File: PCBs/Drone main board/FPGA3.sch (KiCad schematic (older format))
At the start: 11 parts, among them U1201 10CL040_F484, X1401 SiT2001B1-S2-33E-50

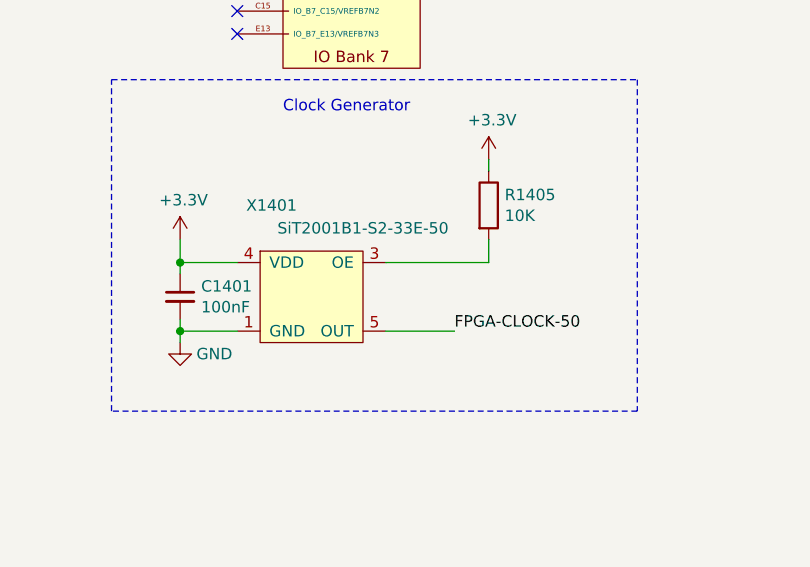
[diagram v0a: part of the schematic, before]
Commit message: Minor tweaks. Improved groundplane around FPGA core (removed and relocated a few power vias) and flipped clock circuit to the same side as the FPGA.
Signed-off-by: Eldalote.Electronics <Eldalote.Electronics@gmail.com>
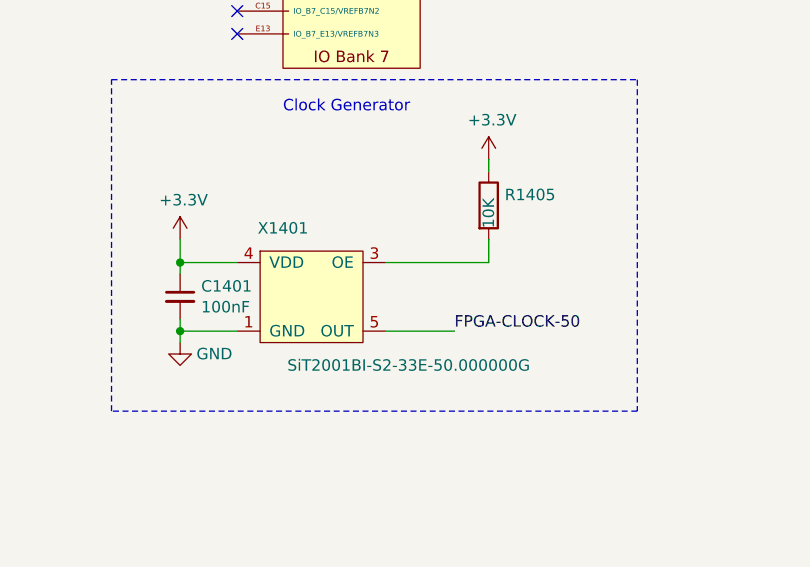
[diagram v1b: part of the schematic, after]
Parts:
- C1401: footprint Inductor_SMD:L_0402_1005Metric -> Inductor_SMD:L_0603_1608Metric_Pad1.05x0.95mm_HandSolder; DigiKey (none) -> 732-13187-1-ND; LCSC C1525 -> (none); Mouser (none) -> 710-885382206004
- X1401: value SiT2001B1-S2-33E-50 -> SiT2001BI-S2-33E-50.000000G; DigiKey (none) -> 1473-SIT2001BI-S2-33E-50.000000G-ND; Mouser (none) -> 788-2001BI-S233E-50G
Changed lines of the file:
@@
 U 1 1 5FC5708A
 P 8200 5400
-F 0 "X1401" H 8200 5300 50  0000 C CNN
-F 1 "SiT2001B1-S2-33E-50" H 8600 5200 50  0000 C CNN
+F 0 "X1401" H 8250 5200 50  0000 C CNN
+F 1 "SiT2001BI-S2-33E-50.000000G" H 8800 4600 50  0000 C CNN
 F 2 "Package_TO_SOT_SMD:SOT-23-5_HandSoldering" H 8200 5400 50  0001 C CNN
 F 3 "" H 8200 5400 50  0001 C CNN
+F 4 "1473-SIT2001BI-S2-33E-50.000000G-ND " H 8200 5400 50  0001 C CNN "DigiKey"
+F 5 "788-2001BI-S233E-50G " H 8200 5400 50  0001 C CNN "Mouser"
 	1    8200 5400
 	1    0    0    -1
@@
 F 0 "C1401" H 7892 5946 50  0000 L CNN
 F 1 "100nF" H 7892 5855 50  0000 L CNN
-F 2 "Inductor_SMD:L_0402_1005Metric" H 7800 5900 50  0001 C CNN
+F 2 "Inductor_SMD:L_0603_1608Metric_Pad1.05x0.95mm_HandSolder" H 7800 5900 50  0001 C CNN
 F 3 "~" H 7800 5900 50  0001 C CNN
-F 4 "" H 7800 5900 50  0001 C CNN "DigiKey"
-F 5 "" H 7800 5900 50  0001 C CNN "Mouser"
-F 6 "C1525" H 7800 5900 50  0001 C CNN "LCSC"
+F 4 "732-13187-1-ND " H 7800 5900 50  0001 C CNN "DigiKey"
+F 5 "710-885382206004" H 7800 5900 50  0001 C CNN "Mouser"
 	1    7800 5900
 	1    0    0    -1
@@
 AR Path="/5F48BB5C/5FC89410" Ref="R1405"  Part="1"
 F 0 "R1405" H 9220 5546 50  0000 L CNN
-F 1 "10K" H 9220 5455 50  0000 L CNN
+F 1 "10K" V 9150 5400 50  0000 L CNN
 F 2 "Resistor_SMD:R_0402_1005Metric" V 9080 5500 50  0001 C CNN
 F 3 "~" H 9150 5500 50  0001 C CNN

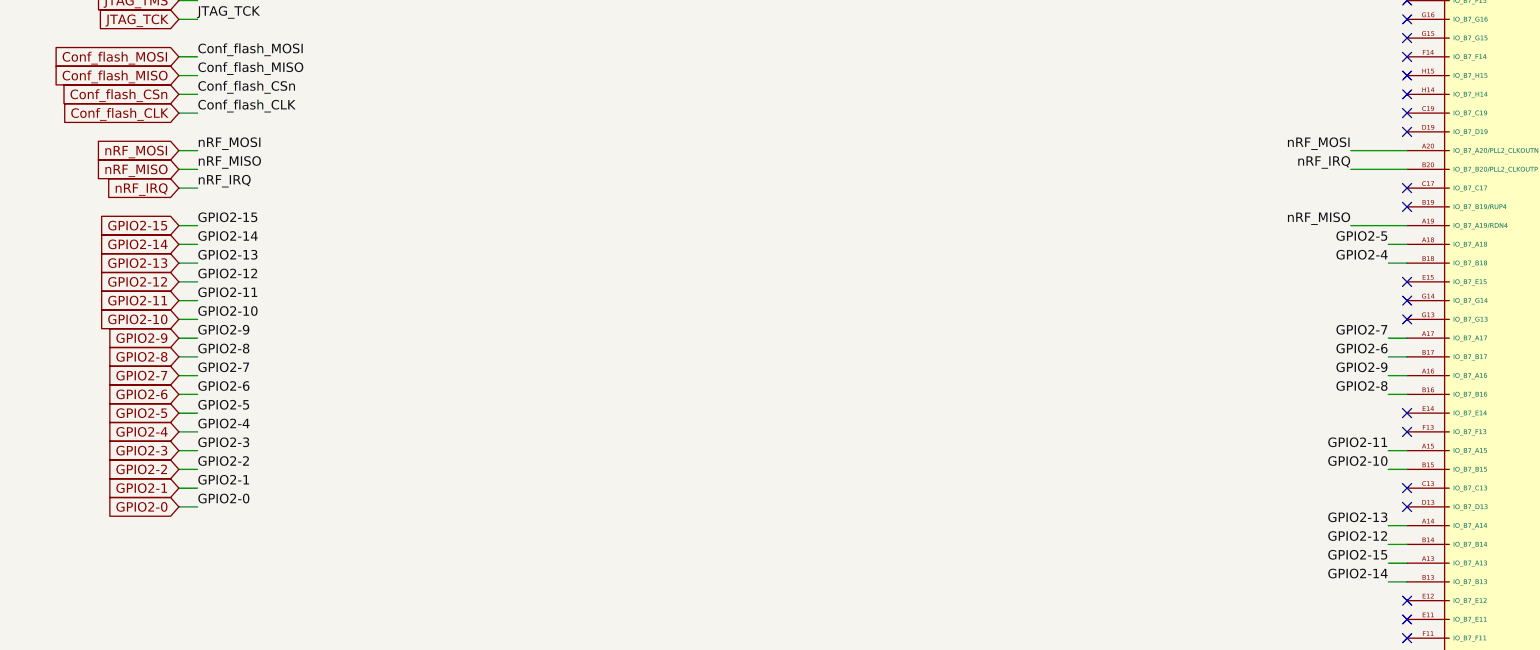
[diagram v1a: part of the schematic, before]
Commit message: Finished (?) the schematic check and update. Next: PCB update
Signed-off-by: Eldalote.Electronics <Eldalote.Electronics@gmail.com>
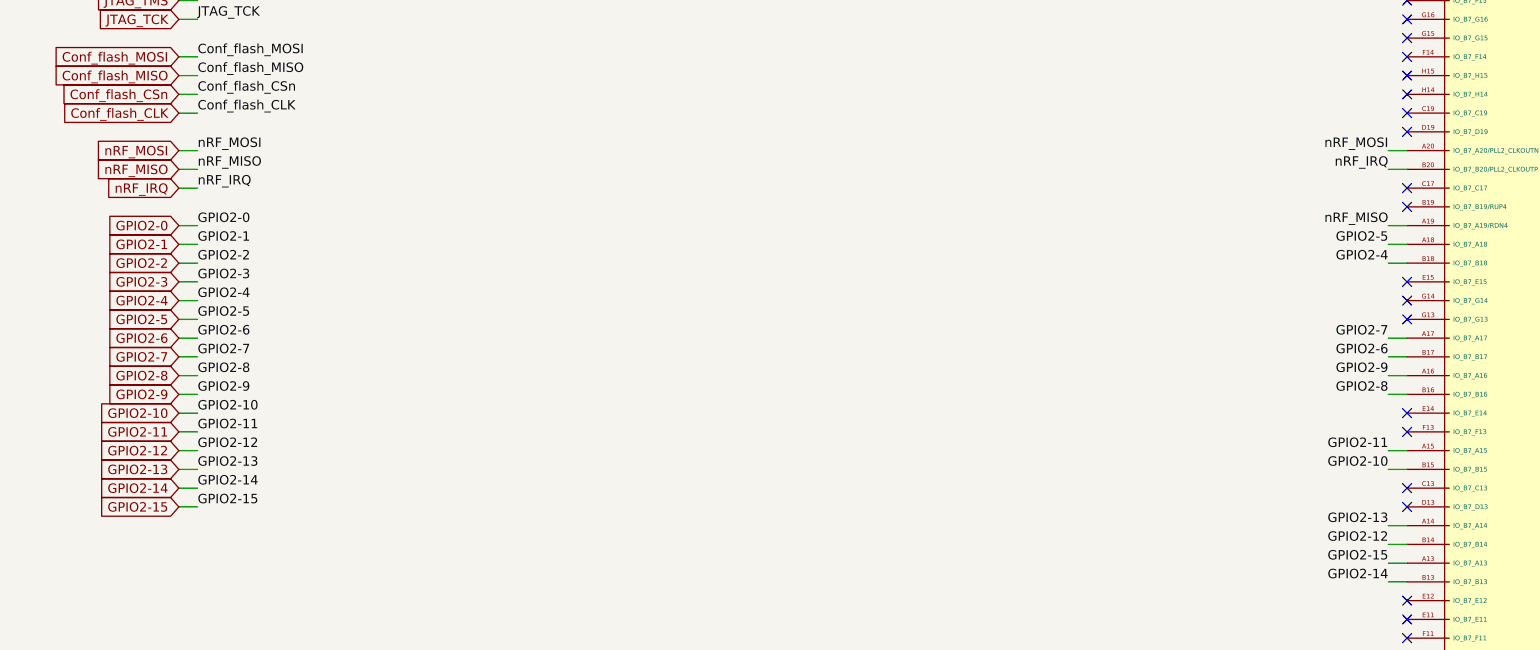
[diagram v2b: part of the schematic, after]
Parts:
- C1401: footprint Inductor_SMD:L_0603_1608Metric_Pad1.05x0.95mm_HandSolder -> Inductor_SMD:L_0402_1005Metric; DigiKey 732-13187-1-ND -> (none); MfNr (none) -> CL05B104KO5NNNC; Mouser 710-885382206004 -> (none)
- R1401, R1402, R1403, R1404, R1405: LCSC C25744 -> (none); MfNr (none) -> RC0402FR-0710KL
- U1201: MfNr (none) -> 10CL040Y
- X1401: footprint Package_TO_SOT_SMD:SOT-23-5_HandSoldering -> Package_TO_SOT_SMD:SOT-23-5; DigiKey 1473-SIT2001BI-S2-33E-50.000000G-ND -> (none); MfNr (none) -> SIT2001BI-S2-33E-50.000000G; Mouser 788-2001BI-S233E-50G -> (none)
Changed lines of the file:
@@
 F 4 "TRUE" H 9300 -5415 35  0001 L CNN "SPLIT_INST"
 F 5 "(S1+S2+S3+S4+S5+S6+S7+S8+S9+S10+S11+S12+S13)" H 9300 -5460 35  0001 L CNN "SWAP_INFO"
+F 6 "10CL040Y" H 8250 600 50  0001 C CNN "MfNr"
 	8    8250 600
 	1    0    0    -1
@@
 F 4 "TRUE" H 11500 -5415 35  0001 L CNN "SPLIT_INST"
 F 5 "(S1+S2+S3+S4+S5+S6+S7+S8+S9+S10+S11+S12+S13)" H 11500 -5460 35  0001 L CNN "SWAP_INFO"
+F 6 "10CL040Y" H 10450 600 50  0001 C CNN "MfNr"
 	9    10450 600
 	1    0    0    -1
@@
 F 4 "TRUE" H 7150 -665 35  0001 L CNN "SPLIT_INST"
 F 5 "(S1+S2+S3+S4+S5+S6+S7+S8+S9+S10+S11+S12+S13)" H 7150 -710 35  0001 L CNN "SWAP_INFO"
+F 6 "10CL040Y" H 6100 5350 50  0001 C CNN "MfNr"
 	10   6100 5350
 	1    0    0    -1
@@
 F 4 "TRUE" H 3100 -815 35  0001 L CNN "SPLIT_INST"
 F 5 "(S1+S2+S3+S4+S5+S6+S7+S8+S9+S10+S11+S12+S13)" H 3100 -860 35  0001 L CNN "SWAP_INFO"
+F 6 "10CL040Y" H 2050 5200 50  0001 C CNN "MfNr"
 	11   2050 5200
 	1    0    0    -1
@@
 F 2 "Resistor_SMD:R_0402_1005Metric" V 4080 5500 50  0001 C CNN
 F 3 "~" H 4150 5500 50  0001 C CNN
-F 4 "C25744" V 4150 5500 50  0001 C CNN "LCSC"
+F 4 "RC0402FR-0710KL" V 4150 5500 50  0001 C CNN "MfNr"
 	1    4150 5500
 	-1   0    0    1
@@
 F 2 "Resistor_SMD:R_0402_1005Metric" V 4280 5600 50  0001 C CNN
 F 3 "~" H 4350 5600 50  0001 C CNN
-F 4 "C25744" V 4350 5600 50  0001 C CNN "LCSC"
+F 4 "RC0402FR-0710KL" V 4350 5600 50  0001 C CNN "MfNr"
 	1    4350 5600
 	-1   0    0    1
@@
 F 2 "Resistor_SMD:R_0402_1005Metric" V 1380 5300 50  0001 C CNN
 F 3 "~" H 1450 5300 50  0001 C CNN
-F 4 "C25744" V 1450 5300 50  0001 C CNN "LCSC"
+F 4 "RC0402FR-0710KL" V 1450 5300 50  0001 C CNN "MfNr"
 	1    1450 5300
 	-1   0    0    1
@@
 nRF_IRQ
 Wire Wire Line
-	8050 2050 7750 2050
-Wire Wire Line
-	8050 1650 7750 1650
-Wire Wire Line
-	8050 1750 7750 1750
-Text Label 7750 1650 2    50   ~ 0
+	8050 2050 7950 2050
+Wire Wire Line
+	8050 1650 7950 1650
+Wire Wire Line
+	8050 1750 7950 1750
+Text Label 7950 1650 2    50   ~ 0
 nRF_MOSI
-Text Label 7750 1750 2    50   ~ 0
+Text Label 7950 1750 2    50   ~ 0
 nRF_IRQ
-Text Label 7750 2050 2    50   ~ 0
+Text Label 7950 2050 2    50   ~ 0
 nRF_MISO
 $Comp
@@
 F 2 "Resistor_SMD:R_0402_1005Metric" V 4580 6050 50  0001 C CNN
 F 3 "~" H 4650 6050 50  0001 C CNN
-F 4 "C25744" V 4650 6050 50  0001 C CNN "LCSC"
+F 4 "RC0402FR-0710KL" V 4650 6050 50  0001 C CNN "MfNr"
 	1    4650 6050
 	-1   0    0    1
@@
 ~CE
 Wire Wire Line
-	1500 3550 1600 3550
+	1500 2050 1600 2050
+Wire Wire Line
+	1600 2150 1500 2150
+Wire Wire Line
+	1600 2250 1500 2250
+Wire Wire Line
+	1600 2350 1500 2350
+Wire Wire Line
+	1600 2450 1500 2450
+Wire Wire Line
+	1600 2550 1500 2550
+Wire Wire Line
+	1600 2650 1500 2650
+Wire Wire Line
+	1600 2750 1500 2750
+Wire Wire Line
+	1600 2850 1500 2850
+Wire Wire Line
+	1600 2950 1500 2950
+Wire Wire Line
+	1600 3050 1500 3050
+Wire Wire Line
+	1600 3150 1500 3150
+Wire Wire Line
+	1600 3250 1500 3250
+Wire Wire Line
+	1600 3350 1500 3350
 Wire Wire Line
 	1600 3450 1500 3450
 Wire Wire Line
-	1600 3350 1500 3350
-Wire Wire Line
-	1600 3250 1500 3250
-Wire Wire Line
-	1600 3150 1500 3150
-Wire Wire Line
-	1600 3050 1500 3050
-Wire Wire Line
-	1600 2950 1500 2950
-Wire Wire Line
-	1600 2850 1500 2850
-Wire Wire Line
-	1600 2750 1500 2750
-Wire Wire Line
-	1600 2650 1500 2650
-Wire Wire Line
-	1600 2550 1500 2550
-Wire Wire Line
-	1600 2450 1500 2450
-Wire Wire Line
-	1600 2350 1500 2350
-Wire Wire Line
-	1600 2250 1500 2250
-Wire Wire Line
-	1600 2150 1500 2150
-Wire Wire Line
-	1600 2050 1500 2050
+	1600 3550 1500 3550
+Text Label 1600 2050 0    50   ~ 0
+GPIO2-0
+Text Label 1600 2150 0    50   ~ 0
+GPIO2-1
+Text Label 1600 2250 0    50   ~ 0
+GPIO2-2
+Text Label 1600 2350 0    50   ~ 0
+GPIO2-3
+Text Label 1600 2450 0    50   ~ 0
+GPIO2-4
+Text Label 1600 2550 0    50   ~ 0
+GPIO2-5
+Text Label 1600 2650 0    50   ~ 0
+GPIO2-6
+Text Label 1600 2750 0    50   ~ 0
+GPIO2-7
+Text Label 1600 2850 0    50   ~ 0
+GPIO2-8
+Text Label 1600 2950 0    50   ~ 0
+GPIO2-9
+Text Label 1600 3050 0    50   ~ 0
+GPIO2-10
+Text Label 1600 3150 0    50   ~ 0
+GPIO2-11
+Text Label 1600 3250 0    50   ~ 0
+GPIO2-12
+Text Label 1600 3350 0    50   ~ 0
+GPIO2-13
+Text Label 1600 3450 0    50   ~ 0
+GPIO2-14
 Text Label 1600 3550 0    50   ~ 0
+GPIO2-15
+Text GLabel 1500 2050 0    50   Input ~ 0
 GPIO2-0
-Text Label 1600 3450 0    50   ~ 0
+Text GLabel 1500 2150 0    50   Input ~ 0
 GPIO2-1
-Text Label 1600 3350 0    50   ~ 0
+Text GLabel 1500 2250 0    50   Input ~ 0
 GPIO2-2
-Text Label 1600 3250 0    50   ~ 0
+Text GLabel 1500 2350 0    50   Input ~ 0
 GPIO2-3
-Text Label 1600 3150 0    50   ~ 0
+Text GLabel 1500 2450 0    50   Input ~ 0
 GPIO2-4
-Text Label 1600 3050 0    50   ~ 0
+Text GLabel 1500 2550 0    50   Input ~ 0
 GPIO2-5
-Text Label 1600 2950 0    50   ~ 0
+Text GLabel 1500 2650 0    50   Input ~ 0
 GPIO2-6
-Text Label 1600 2850 0    50   ~ 0
+Text GLabel 1500 2750 0    50   Input ~ 0
 GPIO2-7
-Text Label 1600 2750 0    50   ~ 0
+Text GLabel 1500 2850 0    50   Input ~ 0
 GPIO2-8
-Text Label 1600 2650 0    50   ~ 0
+Text GLabel 1500 2950 0    50   Input ~ 0
 GPIO2-9
-Text Label 1600 2550 0    50   ~ 0
+Text GLabel 1500 3050 0    50   Input ~ 0
 GPIO2-10
-Text Label 1600 2450 0    50   ~ 0
+Text GLabel 1500 3150 0    50   Input ~ 0
 GPIO2-11
-Text Label 1600 2350 0    50   ~ 0
+Text GLabel 1500 3250 0    50   Input ~ 0
 GPIO2-12
-Text Label 1600 2250 0    50   ~ 0
+Text GLabel 1500 3350 0    50   Input ~ 0
 GPIO2-13
-Text Label 1600 2150 0    50   ~ 0
+Text GLabel 1500 3450 0    50   Input ~ 0
 GPIO2-14
-Text Label 1600 2050 0    50   ~ 0
-GPIO2-15
 Text GLabel 1500 3550 0    50   Input ~ 0
-GPIO2-0
-Text GLabel 1500 3450 0    50   Input ~ 0
-GPIO2-1
-Text GLabel 1500 3350 0    50   Input ~ 0
-GPIO2-2
-Text GLabel 1500 3250 0    50   Input ~ 0
-GPIO2-3
-Text GLabel 1500 3150 0    50   Input ~ 0
-GPIO2-4
-Text GLabel 1500 3050 0    50   Input ~ 0
-GPIO2-5
-Text GLabel 1500 2950 0    50   Input ~ 0
-GPIO2-6
-Text GLabel 1500 2850 0    50   Input ~ 0
-GPIO2-7
-Text GLabel 1500 2750 0    50   Input ~ 0
-GPIO2-8
-Text GLabel 1500 2650 0    50   Input ~ 0
-GPIO2-9
-Text GLabel 1500 2550 0    50   Input ~ 0
-GPIO2-10
-Text GLabel 1500 2450 0    50   Input ~ 0
-GPIO2-11
-Text GLabel 1500 2350 0    50   Input ~ 0
-GPIO2-12
-Text GLabel 1500 2250 0    50   Input ~ 0
-GPIO2-13
-Text GLabel 1500 2150 0    50   Input ~ 0
-GPIO2-14
-Text GLabel 1500 2050 0    50   Input ~ 0
 GPIO2-15
 Wire Wire Line
@@
 F 0 "X1401" H 8250 5200 50  0000 C CNN
 F 1 "SiT2001BI-S2-33E-50.000000G" H 8800 4600 50  0000 C CNN
-F 2 "Package_TO_SOT_SMD:SOT-23-5_HandSoldering" H 8200 5400 50  0001 C CNN
+F 2 "Package_TO_SOT_SMD:SOT-23-5" H 8200 5400 50  0001 C CNN
 F 3 "" H 8200 5400 50  0001 C CNN
-F 4 "1473-SIT2001BI-S2-33E-50.000000G-ND " H 8200 5400 50  0001 C CNN "DigiKey"
-F 5 "788-2001BI-S233E-50G " H 8200 5400 50  0001 C CNN "Mouser"
+F 4 "SIT2001BI-S2-33E-50.000000G" H 8200 5400 50  0001 C CNN "MfNr"
 	1    8200 5400
 	1    0    0    -1
@@
 F 0 "C1401" H 7892 5946 50  0000 L CNN
 F 1 "100nF" H 7892 5855 50  0000 L CNN
-F 2 "Inductor_SMD:L_0603_1608Metric_Pad1.05x0.95mm_HandSolder" H 7800 5900 50  0001 C CNN
+F 2 "Inductor_SMD:L_0402_1005Metric" H 7800 5900 50  0001 C CNN
 F 3 "~" H 7800 5900 50  0001 C CNN
-F 4 "732-13187-1-ND " H 7800 5900 50  0001 C CNN "DigiKey"
-F 5 "710-885382206004" H 7800 5900 50  0001 C CNN "Mouser"
+F 4 "CL05B104KO5NNNC" H 7800 5900 50  0001 C CNN "MfNr"
 	1    7800 5900
 	1    0    0    -1
@@
 F 2 "Resistor_SMD:R_0402_1005Metric" V 9080 5500 50  0001 C CNN
 F 3 "~" H 9150 5500 50  0001 C CNN
-F 4 "" H 9150 5500 50  0001 C CNN "Mouser"
-F 5 "" H 9150 5500 50  0001 C CNN "DigiKey"
-F 6 "C25744" H 9150 5500 50  0001 C CNN "LCSC"
+F 4 "RC0402FR-0710KL" H 9150 5500 50  0001 C CNN "MfNr"
 	1    9150 5500
 	1    0    0    -1
